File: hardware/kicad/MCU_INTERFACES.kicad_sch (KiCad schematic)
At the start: 0 parts

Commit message: feat: mcu interfaces & motor connections
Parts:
- added R9: R, symbol Device:R
- added U3: NUCLEO64-F411RE, Module:ST_Morpho_Connector_144_STLink, symbol MCU_Module:NUCLEO64-F411RE
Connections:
- new net GND_LOGIC: U3.19 (GND), U3.20 (GND), U3.22 (GND), U3.47 (GND), U3.58 (GND), U3.77 (GND), U3.78 (GND), U3.79 (GND), U3.8 (GND), U3.80 (GND)
- new net M1_DIR: U3.69 (STLINK_SWO/PB3)
- new net M1_EN: U3.67 (PB5)
- new net M1_FAULT: U3.37 (PC3)
- new net M1_MS1: U3.38 (PC0)
- new net M1_MS2: U3.36 (PC1)
- new net M1_MS3: U3.35 (PC2)
- new net M1_STEP: U3.61 (PA8)
- new net M2_DIR: U3.65 (PB4)
- new net M2_EN: U3.55 (PB6)
- new net M2_FAULT: U3.62 (PB1)
- new net M2_MS1: U3.72 (PC4)
- new net M2_MS2: U3.44 (PC5)
- new net M2_MS3: U3.2 (PC11)
- new net M2_STEP: U3.59 (PA9)
- new net M3_DIR: U3.21 (PB7)
- new net M3_EN: U3.41 (PB8)
- new net M3_FAULT: U3.40 (PC8)
- new net M3_MS1: U3.43 (PB9)
- new net M3_MS2: U3.42 (PC6)
- new net M3_MS3: U3.57 (PC7)
- new net M3_STEP: U3.71 (PA10)
- new net M4_DIR: U3.54 (PB12)
- new net M4_EN: U3.68 (PB13)
- new net M4_FAULT: U3.1 (PC10)
- new net M4_MS1: U3.66 (PB14)
- new net M4_MS2: U3.64 (PB15)
- new net M4_MS3: U3.39 (PC9)
- new net M4_STEP: U3.63 (PB10)
- new net RPI_INT: U3.34 (PB0)
- new net SPI1_MISO: U3.51 (PA6)
- new net SPI1_MOSI: U3.53 (PA7)
- new net SPI1_NSS: R9.2, U3.32 (PA4)
- new net SPI1_SCK: U3.49 (PA5)
- new net V3V3_LOGIC: R9.1, U3.16 (+3V3)

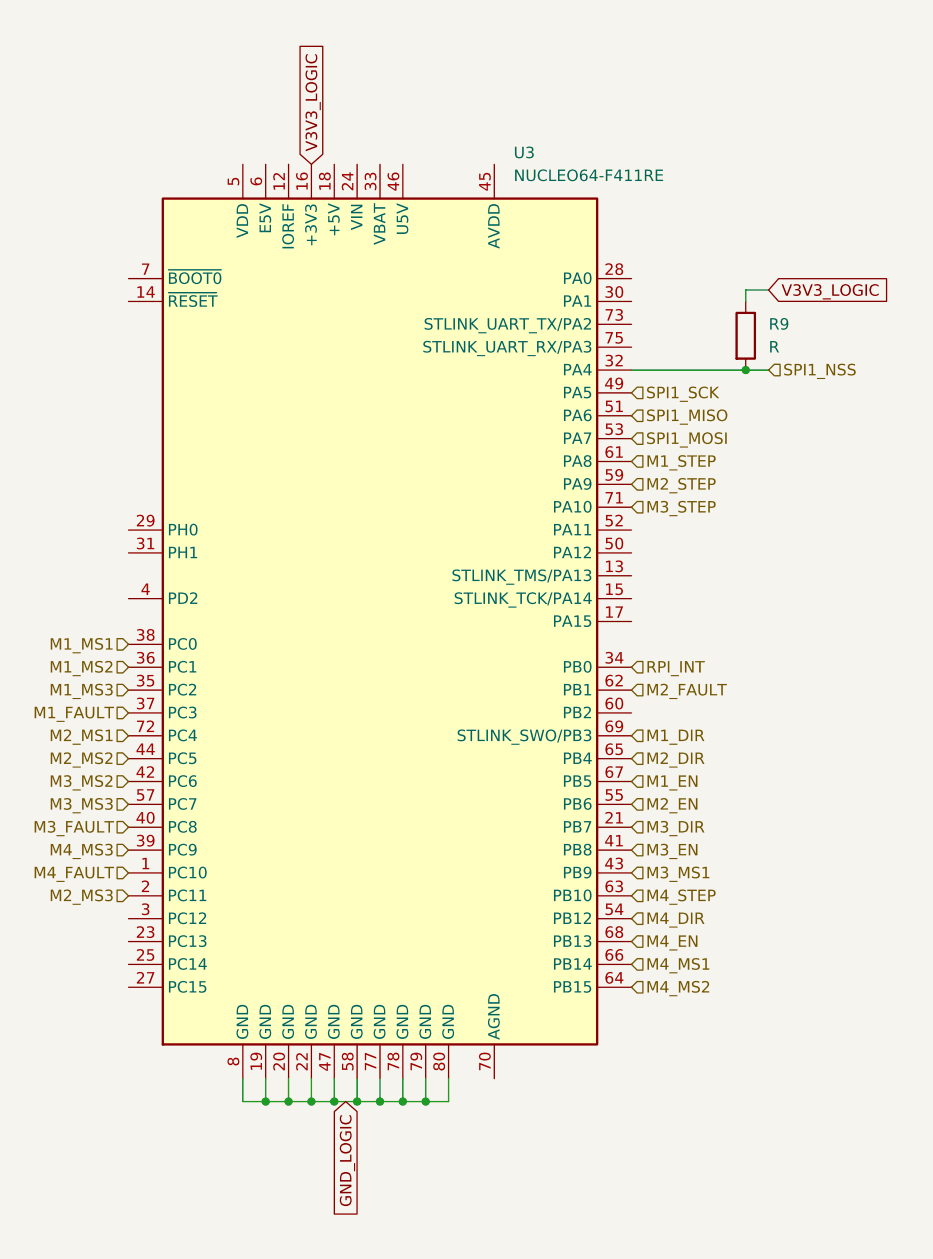
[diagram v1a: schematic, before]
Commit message: fix: error fixing & connection config
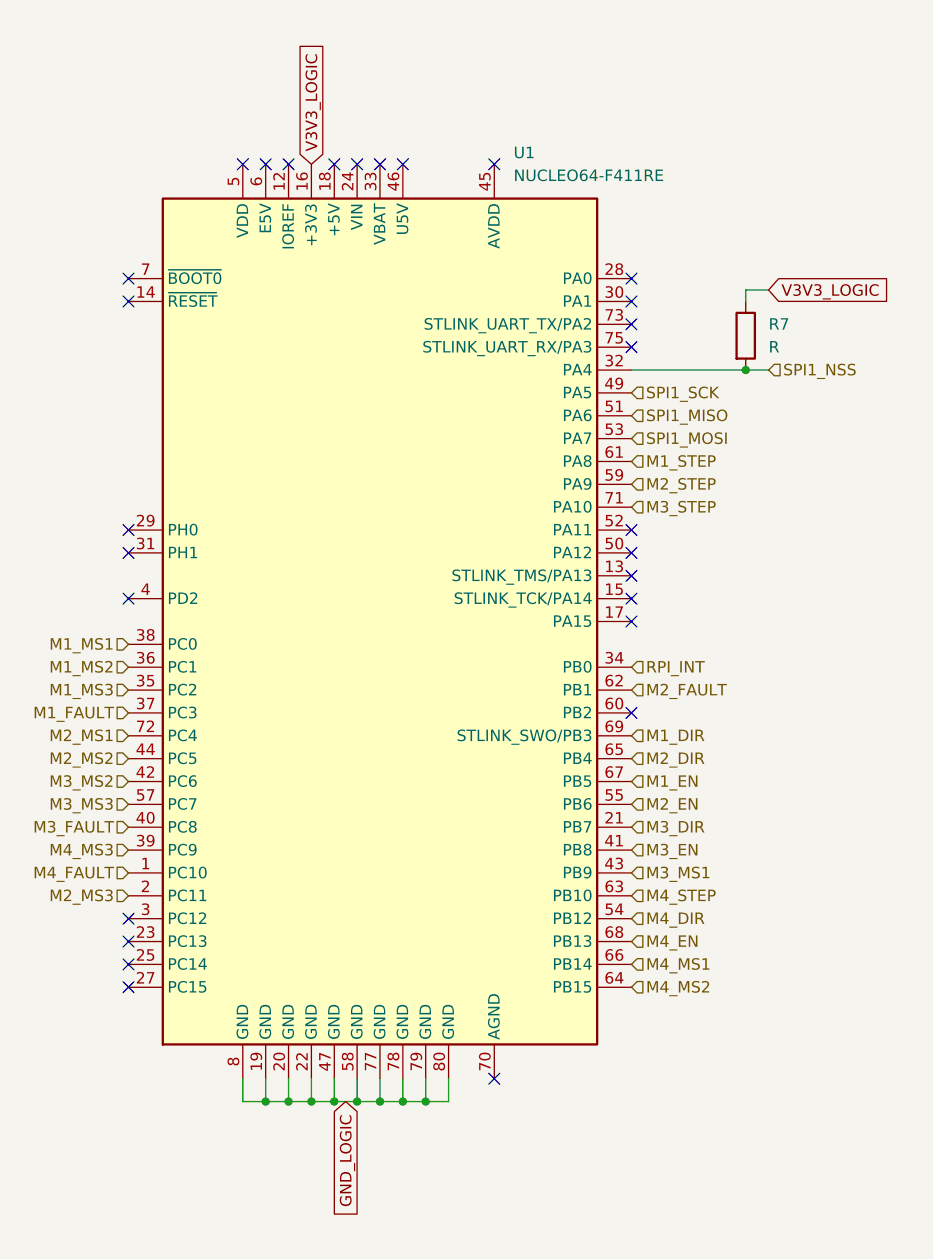
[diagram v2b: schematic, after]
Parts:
- renumbered R9 to R7, U3 to U1
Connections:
- no-connect marks 0 -> 28
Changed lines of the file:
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@@
 		(color 0 0 0 0)
+	)
+	(no_connect
+		(at 101.6 48.26)
+	)
+	(no_connect
+		(at 71.12 63.5)
+	)
+	(no_connect
+		(at 127 60.96)
+	)
+	(no_connect
+		(at 96.52 48.26)
+	)
+	(no_connect
+		(at 83.82 48.26)
+	)
+	(no_connect
+		(at 127 96.52)
+	)
+	(no_connect
+		(at 71.12 96.52)
+	)
+	(no_connect
+		(at 88.9 48.26)
+	)
+	(no_connect
+		(at 71.12 91.44)
+	)
+	(no_connect
+		(at 71.12 139.7)
+	)
+	(no_connect
+		(at 127 109.22)
+	)
+	(no_connect
+		(at 127 91.44)
+	)
+	(no_connect
+		(at 127 68.58)
+	)
+	(no_connect
+		(at 127 93.98)
+	)
+	(no_connect
+		(at 127 88.9)
+	)
+	(no_connect
+		(at 93.98 48.26)
+	)
+	(no_connect
+		(at 86.36 48.26)
+	)
+	(no_connect
+		(at 71.12 132.08)
+	)
+	(no_connect
+		(at 71.12 137.16)
+	)
+	(no_connect
+		(at 71.12 88.9)
+	)
+	(no_connect
+		(at 71.12 134.62)
+	)
+	(no_connect
+		(at 111.76 149.86)
+	)
+	(no_connect
+		(at 127 63.5)
+	)
+	(no_connect
+		(at 127 99.06)
+	)
+	(no_connect
+		(at 71.12 60.96)
+	)
+	(no_connect
+		(at 111.76 48.26)
+	)
+	(no_connect
+		(at 99.06 48.26)
+	)
+	(no_connect
+		(at 127 66.04)
 	)
 	(wire
@@
 		(dnp no)
 		(fields_autoplaced yes)
-		(property "Reference" "R9"
+		(property "Reference" "R7"
 			(at 142.24 66.0399 0)
 			(effects
@@
 			(project ""
 				(path "/0357579f-0f06-4880-b651-8e2778a9baa9/a13f253e-71a8-4833-b68d-03efe6f424dd"
-					(reference "R9")
+					(reference "R7")
 					(unit 1)
 				)
@@
 		(dnp no)
 		(fields_autoplaced yes)
-		(property "Reference" "U3"
+		(property "Reference" "U1"
 			(at 113.9033 46.99 0)
 			(effects
@@
 			(project ""
 				(path "/0357579f-0f06-4880-b651-8e2778a9baa9/a13f253e-71a8-4833-b68d-03efe6f424dd"
-					(reference "U3")
+					(reference "U1")
 					(unit 1)
 				)

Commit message: docs: added end semester report for project
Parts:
- R7: symbol Device:R -> TPSM82903:R
- U1: symbol MCU_Module:NUCLEO64-F411RE -> TPSM82903:NUCLEO64-F411RE
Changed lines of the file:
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@@
 	)
 	(symbol
-		(lib_id "Device:R")
+		(lib_id "TPSM82903:R")
 		(at 139.7 67.31 0)
 		(unit 1)
@@
 	)
 	(symbol
-		(lib_id "MCU_Module:NUCLEO64-F411RE")
+		(lib_id "TPSM82903:NUCLEO64-F411RE")
 		(at 99.06 99.06 0)
 		(unit 1)
